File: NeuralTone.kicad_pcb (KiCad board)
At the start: 2 copper layers, 98 parts, among them J1 USB-C PD, J2 Guitar, J3 Headphones, J4 USB-A Port, J5 Line Out, J6 5V Fan, J7 TF-01A, J8 DF40HC(3.0)-100DS, J9 DF40HC(3.0)-100DS, Q1 AON7421, Q2 IRLML6344, SW1 SW_Push, U1 AP2125N-3.3, U2 CH224K, U3 TLV70245, U4 MCP6022, U5 AP2125N-3.3, U6 AP2151, U7 NAU8814YG, U8 DRTR5V0U2SR, Y1 OT322512MJBA4SL

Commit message: fix all footprints and 3d models
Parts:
- removed R33, R34: 330, Resistor_SMD:R_0805_2012Metric_Pad1.20x1.40mm_HandSolder
- removed U8: DRTR5V0U2SR, Package_TO_SOT_SMD:SOT-143_Handsoldering
- added C31: 100n, Capacitor_SMD:C_0805_2012Metric_Pad1.18x1.45mm_HandSolder, F.Cu at (138.0, 86.4)
- added C32: 4.7u, Capacitor_SMD:C_0805_2012Metric_Pad1.18x1.45mm_HandSolder, F.Cu at (138.0, 89.4)
- added U9: DRTR5V0U2SR, NeuralTone:SOT-143, F.Cu at (163.1, 115.4)
- C10: value 100n -> 4.7u
- C12, C7: value 1u -> 10u; footprint Capacitor_SMD:C_0805_2012Metric_Pad1.18x1.45mm_HandSolder -> Capacitor_SMD:CP_Elec_4x5.8
- C13: value 1u -> 150u; footprint Capacitor_SMD:C_0805_2012Metric_Pad1.18x1.45mm_HandSolder -> Capacitor_SMD:CP_Elec_6.3x7.7
- C14, C15: value 47u -> 1u; footprint Capacitor_SMD:C_1210_3225Metric_Pad1.33x2.70mm_HandSolder -> Capacitor_SMD:C_0805_2012Metric_Pad1.18x1.45mm_HandSolder
- C16, C17: value 4.7u -> 47u; footprint Capacitor_SMD:C_0805_2012Metric_Pad1.18x1.45mm_HandSolder -> Capacitor_SMD:C_1210_3225Metric_Pad1.33x2.70mm_HandSolder
- C18: value 2200u -> 4.7u; footprint Capacitor_SMD:CP_Elec_10x10 -> Capacitor_SMD:C_0805_2012Metric_Pad1.18x1.45mm_HandSolder
- C19, C27: value 33p -> 4.7u
- C20: value 33p -> 2200u; footprint Capacitor_SMD:C_0805_2012Metric_Pad1.18x1.45mm_HandSolder -> Capacitor_SMD:CP_Elec_10x10
- C21, C30: value 4.7u -> 33p
- C22: value 150u -> 33p; footprint Capacitor_SMD:CP_Elec_6.3x7.7 -> Capacitor_SMD:C_0805_2012Metric_Pad1.18x1.45mm_HandSolder
- C24: value 4.7u -> 150u; footprint Capacitor_SMD:C_0805_2012Metric_Pad1.18x1.45mm_HandSolder -> Capacitor_SMD:CP_Elec_6.3x7.7
- C25: value 4.7u -> 10u; footprint Capacitor_SMD:C_0805_2012Metric_Pad1.18x1.45mm_HandSolder -> Capacitor_SMD:CP_Elec_4x5.8
- C26: footprint Capacitor_SMD:CP_Elec_4x5.7 -> Capacitor_SMD:C_0805_2012Metric_Pad1.18x1.45mm_HandSolder
- C28: value 33p -> 10u; footprint Capacitor_SMD:C_0805_2012Metric_Pad1.18x1.45mm_HandSolder -> Capacitor_SMD:CP_Elec_4x5.8
- C29: value 100n -> 33p
- C4: value 100n -> 1u; footprint Capacitor_SMD:C_1206_3216Metric_Pad1.33x1.80mm_HandSolder -> Capacitor_SMD:C_0805_2012Metric_Pad1.18x1.45mm_HandSolder
- C5: value 4.7u -> 1u; footprint Capacitor_SMD:CP_Elec_4x5.7 -> Capacitor_SMD:C_0805_2012Metric_Pad1.18x1.45mm_HandSolder
- C6: value 1u -> 100n; footprint Capacitor_SMD:C_0805_2012Metric_Pad1.18x1.45mm_HandSolder -> Capacitor_SMD:C_1206_3216Metric_Pad1.33x1.80mm_HandSolder
- C8: value 4.7u -> 100n
- D1, D8: footprint Diode_SMD:D_SOD-123 -> NeuralTone:D_SOD-123
- D10, D6: footprint Package_TO_SOT_SMD:SOT-23-6_Handsoldering -> Package_TO_SOT_SMD:SOT-23-6
- D2: value SMF5.0A -> SMF9.0A; footprint Diode_SMD:D_SOD-123F -> NeuralTone:D_SOD-123F
- D4, D5: footprint Diode_SMD:D_SOD-123F -> NeuralTone:D_SOD-123F
- J1: footprint Connector_USB:USB_C_Receptacle_G-Switch_GT-USB-7010ASV -> NeuralTone:USB_C_Receptacle_G-Switch_GT-USB-7010ASV
- J2, J3, J5: footprint Connector_Audio:Jack_6.35mm_Neutrik_NMJ6HCD2_Horizontal -> NeuralTone:Jack_6.35mm_Neutrik_NMJ6HCD2_Horizontal
- J4: footprint Connector_USB:USB_A_CONNFLY_DS1095-WNR0 -> NeuralTone:USB_A_CONNFLY_DS1095-WNR0
- L1: value 104CDMCCDS 4.7u -> 0412CDMCCDS-R10MC; footprint NeuralTone:104CDMCC_DS -> NeuralTone:L_Sunlord_MWSA0412S
- Q2: footprint Package_TO_SOT_SMD:SOT-23-3 -> Package_TO_SOT_SMD:SOT-23
- R10: value 220m -> 10k
- R11: value 220m -> 470k
- R12: value 1k -> 10k
- R13, R6: value 470k -> 10k
- R14, R15: value 10k -> 22
- R18, R30: value 22 -> 10k
- R19: value 22 -> 470k
- R2: value 10k -> 1.8k
- R21: value 470k -> 22
- R22, R9: value 10k -> 1k
- R24, R27: value 1k -> 22
- R25, R29: value 22 -> 1k
- R3: value 1.8k -> 3.9k
- R31: value 1k -> 330
- R32: value 10k -> 330
- R4: value 3.9k -> 470k
- R5: value 10k -> 2.2M
- R7: value 2.2M -> 100m
- R8: value 10k -> 100m
- U1: value AP2125N-3.3 -> AP2210N-3.3
- U2: value CH224K -> AP2210N-5.0; footprint NeuralTone:CH224K -> Package_TO_SOT_SMD:SOT-23
- U3: value TLV70245 -> CH224K; footprint Package_TO_SOT_SMD:SOT-23-5 -> NeuralTone:CH224K
- U5: value AP2125N-3.3 -> AMS1084CM-5.0; footprint Package_TO_SOT_SMD:SOT-23 -> Package_TO_SOT_SMD:TO-263-3_TabPin2
- U6: value AP2151 -> AP2210N-3.3; footprint Package_TO_SOT_SMD:SOT-23-5_HandSoldering -> Package_TO_SOT_SMD:SOT-23
- U7: value NAU8814YG -> AP2171; footprint Package_DFN_QFN:QFN-24-1EP_4x4mm_P0.5mm_EP2.6x2.6mm_ThermalVias -> Package_TO_SOT_SMD:SOT-23-5
- Y1: footprint Crystal:Crystal_SMD_3225-4Pin_3.2x2.5mm -> NeuralTone:Crystal_SMD_3225-4Pin_3.2x2.5mm
- moved R31 119.3 mm to (95.0, 139.6)
- moved R32 119.3 mm to (95.0, 142.6)
- moved U3 111.2 mm to (105.1, 119.4)
- moved C17 104.6 mm to (112.2, 122.5)
- moved C16 103.9 mm to (112.2, 118.3)
- moved C25 95.1 mm to (125.1, 111.5)
- moved C28 95.0 mm to (125.1, 117.4)
- moved C6 93.0 mm to (124.2, 122.0)
- moved C12 89.5 mm to (125.1, 105.7)
- moved Q1 84.4 mm to (131.7, 121.8)
- moved C22 83.9 mm to (133.2, 86.4)
- moved U7 81.9 mm to (143.2, 120.4)
- moved C23 79.6 mm to (133.2, 89.4)
- moved C11 78.1 mm to (128.4, 86.4)
- moved C27 78.1 mm to (133.2, 95.4)
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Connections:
- C1 pad 2: /VDD -> Net-(U3-VDD)
- C10 pad 1: Net-(Q1-D) -> GND
- C10 pad 2: Net-(Q1-G) -> Net-(U4A-+)
- C11 pad 2: +3V3A_B -> +3.3VA
- C12 pad 1: +5V -> +9V
- C13 pad 1: +3V3A_C -> +5V
- C14 pad 1: Net-(C14-Pad1) -> +5V
- C15 pad 1: Net-(C15-Pad1) -> +3.3V
- C16 pad 1: +3V3A_C -> Net-(C16-Pad1)
- C17 pad 1: +3V3A_S -> Net-(C17-Pad1)
- C18 pad 1: /HEADPHONES -> +3.3VA
- C18 pad 2: Net-(C18-Pad2) -> GND
- C19 pad 1: GND -> +5VA
- C19 pad 2: Net-(C18-Pad2) -> GND
- C20 pad 1: GND -> /HEADPHONES
- C21 pad 2: Net-(U7-VREF) -> Net-(C20-Pad2)
- C22 pad 1: Net-(J4-VBUS) -> GND
- C22 pad 2: GND -> Net-(C22-Pad2)
- C23 pad 1: +3V3 -> GND
- C23 pad 2: GND -> Net-(U8-VREF)
- C24 pad 1: +3V3 -> Net-(J4-VBUS)
- C26 pad 1: /LINE_OUT -> +3.3V
- C26 pad 2: Net-(C26-Pad2) -> GND
- C27 pad 1: GND -> +3.3V
- C27 pad 2: Net-(C26-Pad2) -> GND
- C28 pad 1: GND -> /LINE_OUT
- C29 pad 1: +3V3 -> GND
- C29 pad 2: GND -> Net-(C28-Pad2)
- C3 pad 1: +3V3A_B -> +3.3VA
- C30 pad 1: +3V3 -> GND
- C30 pad 2: GND -> Net-(C30-Pad2)
- C4 pad 1: Net-(C4-Pad1) -> +9V
- C4 pad 2: Net-(U4B-+) -> GND
- C5 pad 1: Net-(U4B--) -> +5VA
- C5 pad 2: CODEC_AUX -> GND
- C6 pad 1: +5V -> Net-(C6-Pad1)
- C6 pad 2: GND -> Net-(U4B-+)
- C7 pad 1: +3V3A_S -> Net-(U4B--)
- C7 pad 2: GND -> CODEC_AUX
- C8 pad 1: GND -> /VBUS
- C8 pad 2: Net-(U4A-+) -> Net-(Q1-G)
- C9 pad 1: /VBUS -> Net-(Q1-D)
- D1 pad 1: +3V3A_B -> +3.3VA
- D4 pad 2: Net-(C20-Pad2) -> Net-(C22-Pad2)
- D5 pad 2: Net-(C28-Pad2) -> Net-(C30-Pad2)
- D6 pad 6: +3V3 -> +3.3V
- FB1 pad 1: Net-(C18-Pad2) -> Net-(C20-Pad2)
- FB1 pad 2: Net-(C20-Pad2) -> Net-(C22-Pad2)
- FB2 pad 1: Net-(C26-Pad2) -> Net-(C28-Pad2)
- FB2 pad 2: Net-(C28-Pad2) -> Net-(C30-Pad2)
- J3 pad R: Net-(C20-Pad2) -> Net-(C22-Pad2)
- J3 pad T: Net-(C20-Pad2) -> Net-(C22-Pad2)
- J5 pad R: Net-(C28-Pad2) -> Net-(C30-Pad2)
- J5 pad T: Net-(C28-Pad2) -> Net-(C30-Pad2)
- J7 pad 4: +3V3 -> +3.3V
- J8 pad 78: +3V3 -> Net-(J8-GPIO_VREF(1.8v/3.3v_Input))
- J8 pad 84: +3V3 -> Net-(J8-GPIO_VREF(1.8v/3.3v_Input))
- J8 pad 86: +3V3 -> unconnected-(J8-+3.3v_(Output)-Pad86)
- L1 pad 2: +5V -> +9V
- R1 pad 2: /VDD -> Net-(U3-VDD)
- R10 pad 1: Net-(Q1-D) -> GND
- R10 pad 2: Net-(C14-Pad1) -> Net-(U4A-+)
- R11 pad 1: +5V -> Net-(Q1-G)
- R11 pad 2: Net-(C15-Pad1) -> /PG
- R12 pad 1: +5V -> Net-(C20-Pad2)
- R12 pad 2: Net-(D3-A) -> GND
- R13 pad 1: Net-(Q1-G) -> +5V
- R13 pad 2: /PG -> Net-(U7-EN)
- R14 pad 1: Net-(C18-Pad2) -> I2S_DOUT
- R14 pad 2: GND -> Net-(U8-ADCOUT)
- R15 pad 1: +5V -> I2S_DIN
- R15 pad 2: Net-(U6-EN) -> Net-(U8-DACIN)
- R16 pad 1: I2S_DOUT -> I2S_LRCK
- R16 pad 2: Net-(U7-ADCOUT) -> Net-(U8-FS)
- R17 pad 1: I2S_DIN -> I2S_BCK
- R17 pad 2: Net-(U7-DACIN) -> Net-(U8-BCLK)
- R18 pad 1: I2S_LRCK -> Net-(U8-MODE)
- R18 pad 2: Net-(U7-FS) -> GND
- R19 pad 1: I2S_BCK -> Net-(C28-Pad2)
- R19 pad 2: Net-(U7-BCLK) -> GND
- R2 pad 1: Net-(U2-CFG1) -> Net-(J2-PadT)
- R2 pad 2: /VDD -> Net-(D1-A)
- R20 pad 1: Net-(U7-MODE) -> GND
- R20 pad 2: GND -> Net-(U8-CSb/GPIO)
- R21 pad 1: Net-(C26-Pad2) -> SD_DAT2
- R21 pad 2: GND -> Net-(J7-DAT2)
- R22 pad 1: GND -> LED_STAT_1
- R22 pad 2: Net-(U7-CSb/GPIO) -> Net-(D7-A)
- R23 pad 1: SD_DAT2 -> SD_DAT3
- R23 pad 2: Net-(J7-DAT2) -> Net-(J7-DAT3/CD)
- R24 pad 1: LED_STAT_1 -> SD_CMD
- R24 pad 2: Net-(D7-A) -> Net-(J7-CMD)
- R25 pad 1: SD_DAT3 -> LED_STAT_2
- R25 pad 2: Net-(J7-DAT3/CD) -> Net-(D9-A)
- R26 pad 1: SD_CMD -> SD_CLK
- R26 pad 2: Net-(J7-CMD) -> Net-(J7-CLK)
- R27 pad 1: LED_STAT_2 -> SD_DAT0
- R27 pad 2: Net-(D9-A) -> Net-(J7-DAT0)
- R28 pad 1: SD_CLK -> SD_DAT1
- R28 pad 2: Net-(J7-CLK) -> Net-(J7-DAT1)
- R29 pad 1: SD_DAT0 -> FAN_PWM
- R29 pad 2: Net-(J7-DAT0) -> Net-(Q2-G)
- R3 pad 1: Net-(J2-PadT) -> Net-(D1-A)
- R3 pad 2: Net-(D1-A) -> Net-(C6-Pad1)
- R30 pad 1: SD_DAT1 -> Net-(Q2-G)
- R30 pad 2: Net-(J7-DAT1) -> GND
- R31 pad 1: FAN_PWM -> I2C_SCL
- R31 pad 2: Net-(Q2-G) -> Net-(J8-GPIO3)
- R32 pad 1: Net-(Q2-G) -> I2C_SDA
- R32 pad 2: GND -> Net-(J8-GPIO2)
- R4 pad 1: Net-(D1-A) -> CODEC_AUX
- R4 pad 2: Net-(C4-Pad1) -> GND
- R5 pad 1: +5V -> Net-(U4A--)
- R5 pad 2: Net-(U3-EN) -> Net-(U4B-+)
- R6 pad 1: CODEC_AUX -> Net-(U4A-+)
- R6 pad 2: GND -> +3.3VA
- R7 pad 1: Net-(U4A--) -> Net-(Q1-D)
- R7 pad 2: Net-(U4B-+) -> Net-(C16-Pad1)
- R8 pad 1: Net-(U4A-+) -> +9V
- R8 pad 2: +3V3A_B -> Net-(C17-Pad1)
- R9 pad 1: GND -> +9V
- R9 pad 2: Net-(U4A-+) -> Net-(D3-A)
- U1 pad 2: +3V3A_B -> +3.3VA
- U2 pad 1: /VDD -> GND
- U2 pad 2: unconnected-(U2-CFG2-Pad2) -> +5VA
- U2 pad 3: unconnected-(U2-CFG3-Pad3) -> +9V
- U3 pad 1: +5V -> Net-(U3-VDD)
- U3 pad 2: GND -> unconnected-(U3-CFG2-Pad2)
- U3 pad 3: Net-(U3-EN) -> unconnected-(U3-CFG3-Pad3)
- U3 pad 4: unconnected-(U3-NC-Pad4) -> Net-(U3-DM)
- U3 pad 5: +3V3A_S -> Net-(U3-DM)
- U4 pad 8: +3V3A_B -> +3.3VA
- U5 pad 2: +3V3A_C -> +5V
- U5 pad 3: +5V -> +9V
- U6 pad 1: Net-(J4-VBUS) -> GND
- U6 pad 2: GND -> +3.3V
- U6 pad 3: unconnected-(U6-~{FLG}-Pad3) -> +5V
- U7 pad 1: unconnected-(U7-MICBIAS-Pad1) -> Net-(J4-VBUS)
- U7 pad 2: +3V3A_C -> GND
- U7 pad 3: GND -> unconnected-(U7-~{FLG}-Pad3)
- U7 pad 4: +3V3 -> Net-(U7-EN)
- U7 pad 5: +3V3 -> +5V
- Y1 pad 4: +3V3 -> +3.3V

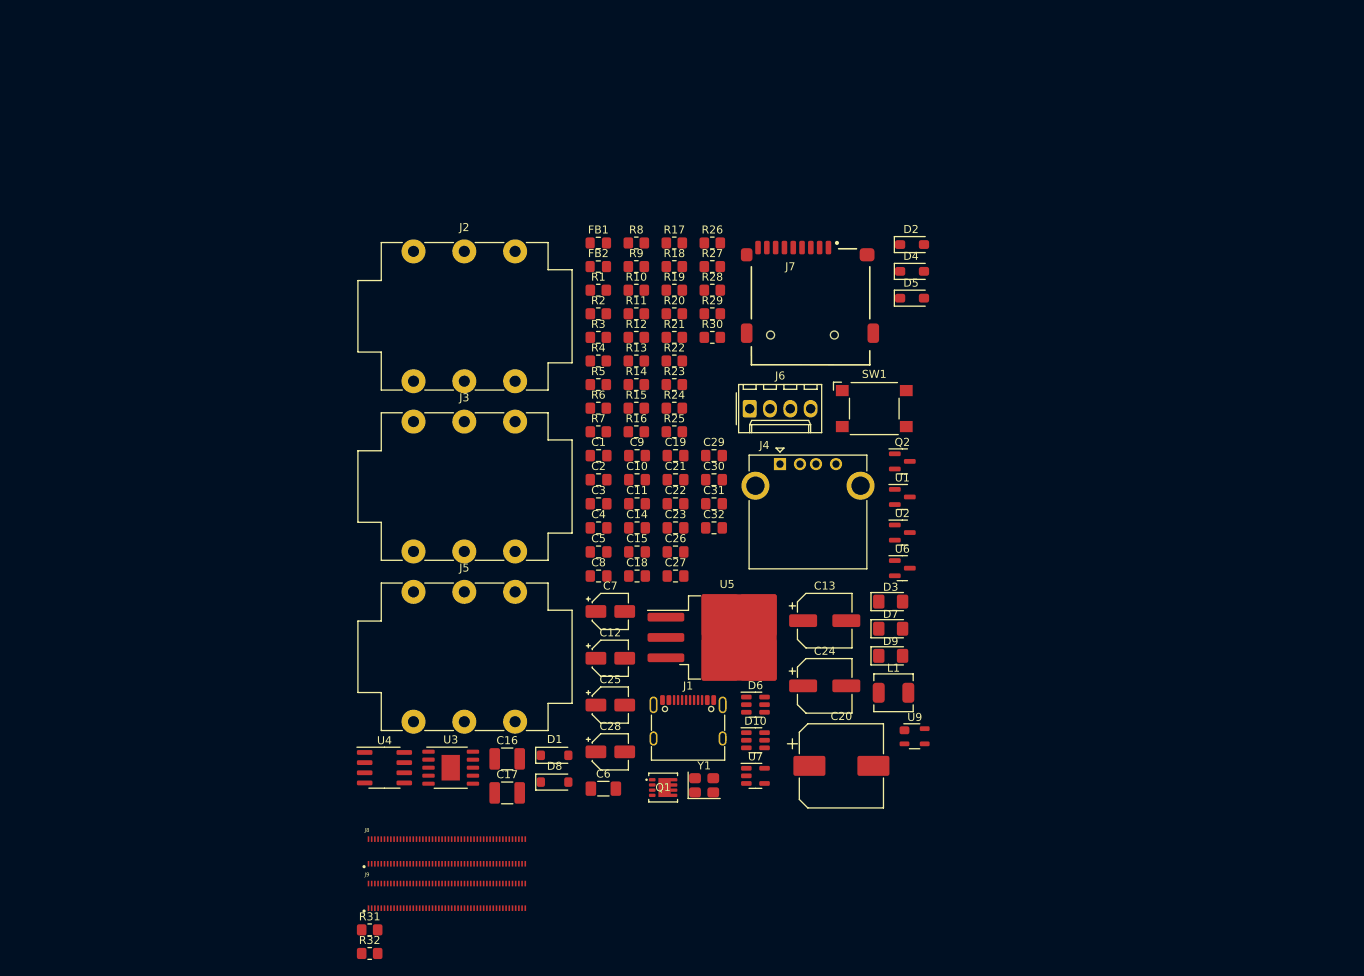
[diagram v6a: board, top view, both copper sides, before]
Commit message: switch to 0603 footprints
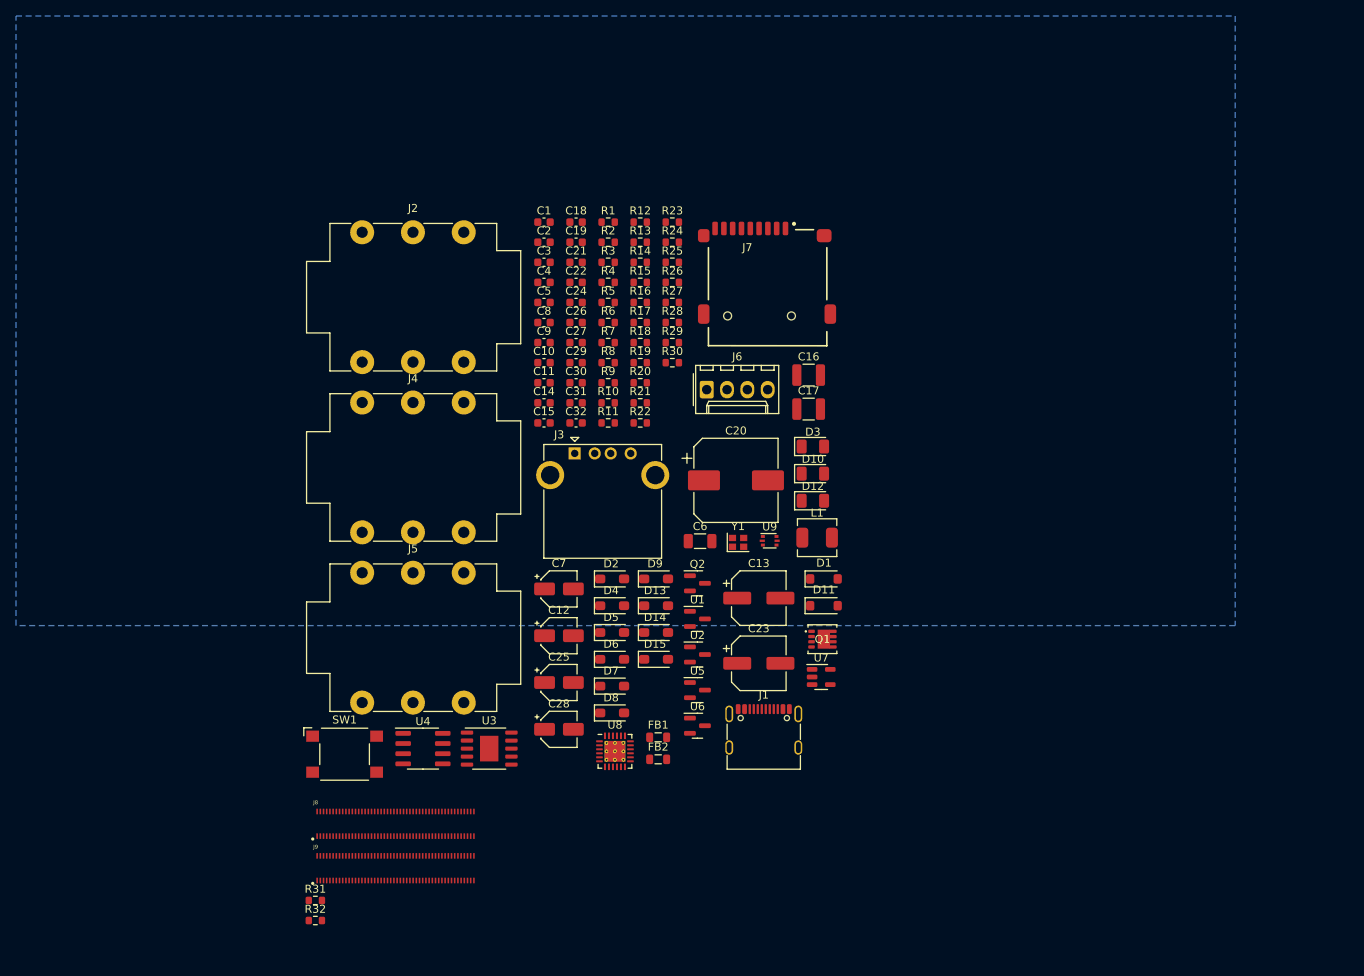
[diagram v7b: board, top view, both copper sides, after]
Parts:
- added D11: 1N4148W, NeuralTone:D_SOD-123, F.Cu at (151.8, 99.1)
- added D12: LED_Small, LED_SMD:LED_1206_3216Metric, F.Cu at (150.4, 86.0)
- added D13: SMF3.3A, NeuralTone:D_SOD-123F, F.Cu at (130.8, 99.1)
- added D14: SMF3.3A, NeuralTone:D_SOD-123F, F.Cu at (130.8, 102.5)
- added D15: SMF3.3A, NeuralTone:D_SOD-123F, F.Cu at (130.8, 105.8)
- added U8: NAU8814YG, Package_DFN_QFN:QFN-24-1EP_4x4mm_P0.5mm_EP2.6x2.6mm_ThermalVias, F.Cu at (125.7, 117.3)
- C1, C10, C11, C14, C18, C19, C2, C21, C22, C26, C27, C29, C30, C31, C32, C4, C8, C9: footprint Capacitor_SMD:C_0805_2012Metric_Pad1.18x1.45mm_HandSolder -> Capacitor_SMD:C_0603_1608Metric
- C15, C3, C5: value 1u -> 4.7u; footprint Capacitor_SMD:C_0805_2012Metric_Pad1.18x1.45mm_HandSolder -> Capacitor_SMD:C_0603_1608Metric
- C16, C17: footprint Capacitor_SMD:C_1210_3225Metric_Pad1.33x2.70mm_HandSolder -> Capacitor_SMD:C_1210_3225Metric
- C23: value 4.7u -> 150u; footprint Capacitor_SMD:C_0805_2012Metric_Pad1.18x1.45mm_HandSolder -> Capacitor_SMD:CP_Elec_6.3x7.7
- C24: value 150u -> 4.7u; footprint Capacitor_SMD:CP_Elec_6.3x7.7 -> Capacitor_SMD:C_0603_1608Metric
- C6: footprint Capacitor_SMD:C_1206_3216Metric_Pad1.33x1.80mm_HandSolder -> Capacitor_SMD:C_1206_3216Metric
- D10: value PESD3V3S4UD -> LED_Small; footprint Package_TO_SOT_SMD:SOT-23-6 -> LED_SMD:LED_1206_3216Metric
- D3: footprint LED_SMD:LED_1206_3216Metric_Pad1.42x1.75mm_HandSolder -> LED_SMD:LED_1206_3216Metric
- D6: value PESD3V3S4UD -> SMF3.3A; footprint Package_TO_SOT_SMD:SOT-23-6 -> NeuralTone:D_SOD-123F
- D7, D9: value LED_Small -> SMF3.3A; footprint LED_SMD:LED_1206_3216Metric_Pad1.42x1.75mm_HandSolder -> NeuralTone:D_SOD-123F
- D8: value 1N4148W -> SMF3.3A; footprint NeuralTone:D_SOD-123 -> NeuralTone:D_SOD-123F
- FB1, FB2: footprint Inductor_SMD:L_0805_2012Metric_Pad1.15x1.40mm_HandSolder -> Inductor_SMD:L_0805_2012Metric
- J3: value Headphones -> USB-A Port; footprint NeuralTone:Jack_6.35mm_Neutrik_NMJ6HCD2_Horizontal -> NeuralTone:USB_A_CONNFLY_DS1095-WNR0
- J4: value USB-A Port -> Headphones; footprint NeuralTone:USB_A_CONNFLY_DS1095-WNR0 -> NeuralTone:Jack_6.35mm_Neutrik_NMJ6HCD2_Horizontal
- R1, R10, R11, R12, R13, R14, R15, R16, R17, R18, R19, R2, R20, R23, R24, R25, R26, R27, R3, R30, R31, R32, R4, R5, R6, R7, R8, R9: footprint Resistor_SMD:R_0805_2012Metric_Pad1.20x1.40mm_HandSolder -> Resistor_SMD:R_0603_1608Metric
- R21, R28: value 22 -> 1k; footprint Resistor_SMD:R_0805_2012Metric_Pad1.20x1.40mm_HandSolder -> Resistor_SMD:R_0603_1608Metric
- R22, R29: value 1k -> 22; footprint Resistor_SMD:R_0805_2012Metric_Pad1.20x1.40mm_HandSolder -> Resistor_SMD:R_0603_1608Metric
- U5: footprint Package_TO_SOT_SMD:TO-263-3_TabPin2 -> Package_TO_SOT_SMD:SOT-23
- U9: value DRTR5V0U2SR -> USBLC6-2P6; footprint NeuralTone:SOT-143 -> Package_TO_SOT_SMD:SOT-666
- Y1: value OT322512MJBA4SL -> OT201624MJBA4SL; footprint NeuralTone:Crystal_SMD_3225-4Pin_3.2x2.5mm -> Crystal:Crystal_SMD_2016-4Pin_2.0x1.6mm
- moved SW1 79.1 mm to (91.9, 117.7)
- moved FB1 62.2 mm to (131.1, 115.6)
- moved FB2 62.0 mm to (131.1, 118.3)
- moved C16 61.0 mm to (149.9, 70.3)
- moved C17 61.0 mm to (149.9, 74.5)
- moved C24 57.1 mm to (120.8, 61.2)
- moved D2 56.1 mm to (125.3, 95.8)
- moved D4 56.1 mm to (125.3, 99.1)
- moved D5 56.1 mm to (125.3, 102.5)
- moved J4 52.8 mm to (94.1, 73.7)
- moved C18 44.9 mm to (120.8, 51.2)
- moved D1 40.2 mm to (151.8, 95.8)
- moved C20 38.0 mm to (140.8, 83.4)
- moved D7 35.6 mm to (125.3, 109.2)
- moved D10 34.1 mm to (150.4, 82.6)
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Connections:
- C23 pad 1: GND -> Net-(J3-VBUS)
- C23 pad 2: Net-(U8-VREF) -> GND
- C24 pad 1: Net-(J4-VBUS) -> GND
- C24 pad 2: GND -> Net-(U8-VREF)
- D10 pad 1: Net-(J7-CLK) -> GND
- D10 pad 2: GND -> Net-(D10-A)
- D6 pad 1: Net-(J7-DAT2) -> Net-(D6-K)
- D7 pad 1: GND -> Net-(D7-K)
- D7 pad 2: Net-(D7-A) -> GND
- D8 pad 1: +5V -> Net-(D8-K)
- D8 pad 2: /PWM -> GND
- D9 pad 1: GND -> +3.3V
- D9 pad 2: Net-(D9-A) -> GND
- J7 pad 1: Net-(J7-DAT2) -> Net-(D6-K)
- J7 pad 2: Net-(J7-DAT3/CD) -> Net-(D7-K)
- J7 pad 3: Net-(J7-CMD) -> Net-(D8-K)
- J7 pad 5: Net-(J7-CLK) -> Net-(D15-K)
- J7 pad 7: Net-(J7-DAT0) -> Net-(D14-K)
- J7 pad 8: Net-(J7-DAT1) -> Net-(D13-K)
- R12 pad 1: Net-(C20-Pad2) -> +5V
- R12 pad 2: GND -> Net-(U7-EN)
- R13 pad 1: +5V -> Net-(C20-Pad2)
- R13 pad 2: Net-(U7-EN) -> GND
- R21 pad 1: SD_DAT2 -> LED_STAT_1
- R21 pad 2: Net-(J7-DAT2) -> Net-(D10-A)
- R22 pad 1: LED_STAT_1 -> SD_DAT2
- R22 pad 2: Net-(D7-A) -> Net-(D6-K)
- R23 pad 2: Net-(J7-DAT3/CD) -> Net-(D7-K)
- R24 pad 2: Net-(J7-CMD) -> Net-(D8-K)
- R25 pad 2: Net-(D9-A) -> Net-(D12-A)
- R26 pad 2: Net-(J7-CLK) -> Net-(D15-K)
- R27 pad 2: Net-(J7-DAT0) -> Net-(D14-K)
- R28 pad 1: SD_DAT1 -> FAN_PWM
- R28 pad 2: Net-(J7-DAT1) -> Net-(Q2-G)
- R29 pad 1: FAN_PWM -> SD_DAT1
- R29 pad 2: Net-(Q2-G) -> Net-(D13-K)
- U7 pad 1: Net-(J4-VBUS) -> Net-(J3-VBUS)
- U9 pad 1: GND -> USBD+
- U9 pad 2: USBD+ -> GND
- U9 pad 3: Net-(J4-VBUS) -> USBD-
- U9 pad 4: USBD- -> Net-(J3-D-)
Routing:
- added copper zone on B.Cu, net GND
